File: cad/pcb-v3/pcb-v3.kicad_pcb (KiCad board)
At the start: 4 copper layers, 19.3 x 19.3 mm, 50 parts

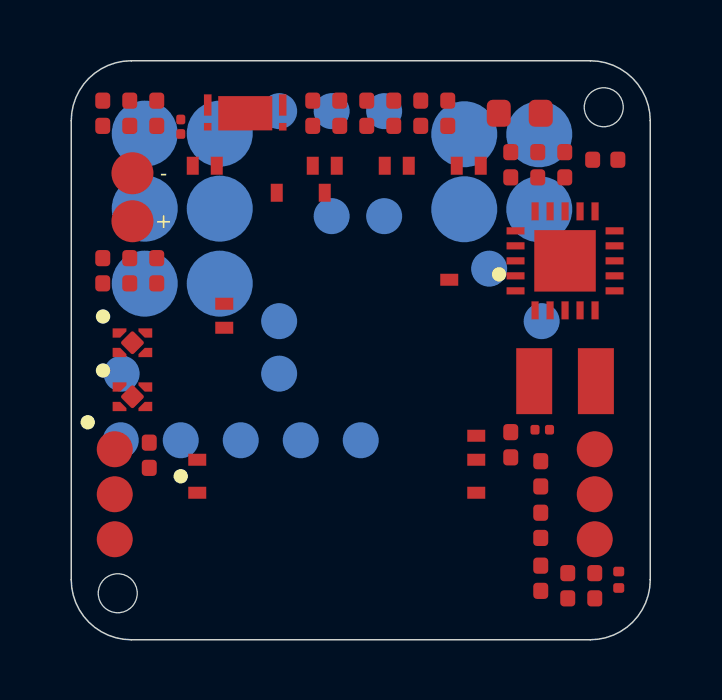
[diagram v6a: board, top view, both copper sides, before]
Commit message: regenerate placement: 20x19 board, caliper pogo datum, press-fit pins
Board is no longer square, so the generator had to learn the difference. Five
SQUARE-BOARD BUGS were hiding behind a single HALF constant, every one of them
silently using an X value where a Y was meant:

  * np.meshgrid(_gx, _gx) built a 20 x 20 grid on a 20 x 19 board
  * the legality mask was np.ones((_NX,_NX)) instead of (_NY,_NX)
  * the index guard tested iy against _NX
  * FIVE sites read _gx[iy] for a Y coordinate -- this is what put a row of
    0402s at y=-9.12, off the board
  * U5's own candidate loop read _gx[_iy], which parked it at y=-8.4 through
    the housing lip wall
  * the Edge.Cuts corner arcs used one  for both axes

None of these could show up while the board was square. BOARD/HALF are now
BOARD_X/BOARD_Y and HALF_X/HALF_Y so the distinction cannot collapse again.

POGO DATUM, from calipers, every measurement closing:
  pad 2.00, pin 1.00, uniform 2.50 pitch (0.50 gap)
  cols x = -6.50, -4.00, +4.00, +6.50   rows y = -8.25, -5.75, -3.25
  board edge -> outer PIN edge 3.00 | between inner PAD edges 6.00
  top PAD edge to -Y edge 0.25 | J4 4.50x7.00 | J11 4.50x4.50
  chain 2.50+4.50+6.00+4.50+2.50 = 20.00 exactly
Pad dia went 2.20 -> 2.00 because the 0.25 edge reading is to the OEM's 2.00
pad; at 2.20 the top row reaches y=-9.35 against a -9.30 limit.

SCREWS -> PRESS-FIT PINS at (-8.75, 0) and (+8.75, 0), i.e. corner-origin
(1.25, 9.50) and (18.75, 9.50) as asked. A pin passes THROUGH the hole, so the
r1.20 plastic boss that used to stand on the board face is gone and the
board-side cost is the hole alone -- which is the only reason these positions
are reachable. BOSS_R is now the hole radius (0.60), not zero: zero would let
the placer park a part on the pin. Hole 1.20 leaves a 0.65 mm web to the edge.

Also fixed a FALSE clearance violation in this file's own checker: it modelled
every pad as an axis-aligned box, which under-reports the gap between two ROUND
pads offset dia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
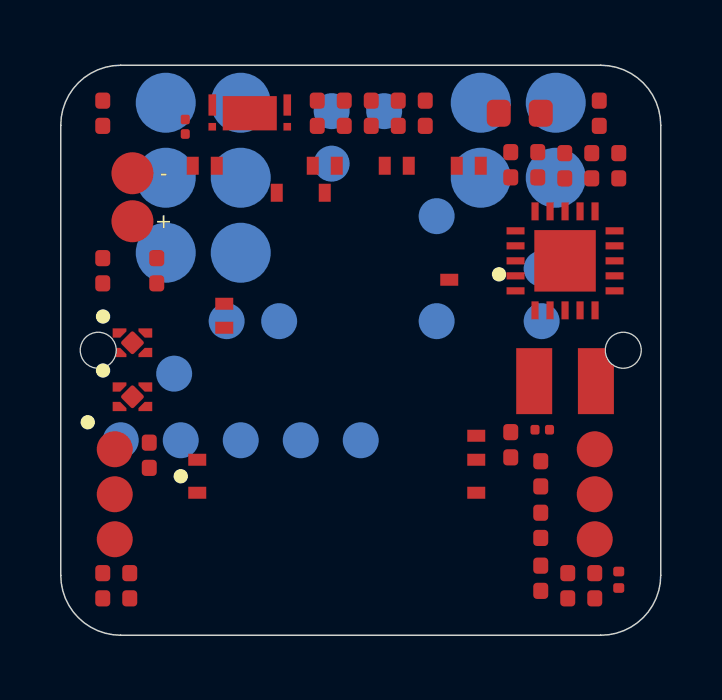
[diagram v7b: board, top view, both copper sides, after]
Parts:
- removed the ? at (8.10, -8.10)
- removed the ? at (-8.10, 8.10)
- added ?: , touchid:MH, F.Cu at (-8.75, 0.00)
- added ?: , touchid:MH, F.Cu at (8.75, 0.00)
- moved R3 18.2 mm to (6.00, 4.12)
- moved R5 17.8 mm to (-8.60, -2.65)
- moved R2 16.5 mm to (7.80, 7.85)
- moved R8 15.7 mm to (6.05, 2.65), turned to 0 degrees
- moved R9 15.6 mm to (-5.85, -7.45), turned to 90 degrees
- moved C3 14.6 mm to (-7.70, 7.85)
- moved ROK1 14.0 mm to (8.60, -6.15)
- moved C5 12.4 mm to (5.00, 3.15)
- moved R1 11.9 mm to (5.00, -6.18)
- moved C12 11.5 mm to (-7.05, 3.50)
- moved R6 9.61 mm to (1.25, -7.90)
- moved R7 8.87 mm to (-0.55, -7.90)
- moved C13 7.00 mm to (-8.60, -7.90)
- moved C10 5.07 mm to (6.90, 7.85)
- moved TP3 4.95 mm to (2.53, -0.97)
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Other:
- board size 19.3 x 19.3 mm -> 20 x 19 mm

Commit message: wire up the PCM cluster constraint that was written but never read
C14 -- the PCM's supply bypass -- was 19.77 mm from U5 on a 20 mm board. Three
things were wrong, all of them latent:

1. SMALL_NEAR = (3.0, 4.5, 6.0, 8.0) existed, and _place_smalls' own comment
   said 'keep them within SMALL_NEAR of U5', but NOTHING EVER READ IT.
   Distance only ever RANKED candidates; it never REJECTED one. With the shelf
   beside U5 full, 'nearest' became the far corner.
2. CLUSTER_OK was 99.0 -- the guard meant to reject a U5 position that
   scatters its cluster was effectively switched off.
3. _place_smalls masked every 0402 SLOT out and hunted leftover space, while
   its own docstring said these parts take slots. There is no leftover space
   next to U5, which is why forcing a radius made every U5 trial fail outright.

Fixed: per-part ladders (C14 tightest, it is the bypass; R8 loosest, its 330
ohm swamps any parasitic), C14 placed FIRST so it takes the best spot rather
than the leftovers, CLUSTER_OK 99 -> 8, and slot centres offered as candidates
with the consumed slot handed back to the packer. Slot candidates are checked
against the real legality mask -- skipping that first put R8 past the 17.94
housing cavity and overlapped C14 with R9.

    C14  19.77 mm -> 3.42     R8  14.31 -> 4.75     R9  2.18 -> 1.95

Routing: PCM_VDD then CELL_NEG then PCM_VM must go BEFORE the rest of stage 1.
With the cluster tight, PCM_VM takes the corridor PCM_VDD needs to reach C14
and PCM_VDD fails. Split into stage 1a (PCM) and 1b (the rest); all route.

New push_off_pads.py: the router lays copper 1-9 microns inside the clearance
rule against ROTATED 0402 pads, on a different net every re-route. Hand-nudging
one segment at a time had been done twice. This finds every grazing track,
computes the shortest perpendicular push, and RE-TESTS the pushed segment
against every foreign pad, track and via before accepting it -- a fix that
trades one violation for another is not a fix. 28 segments p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
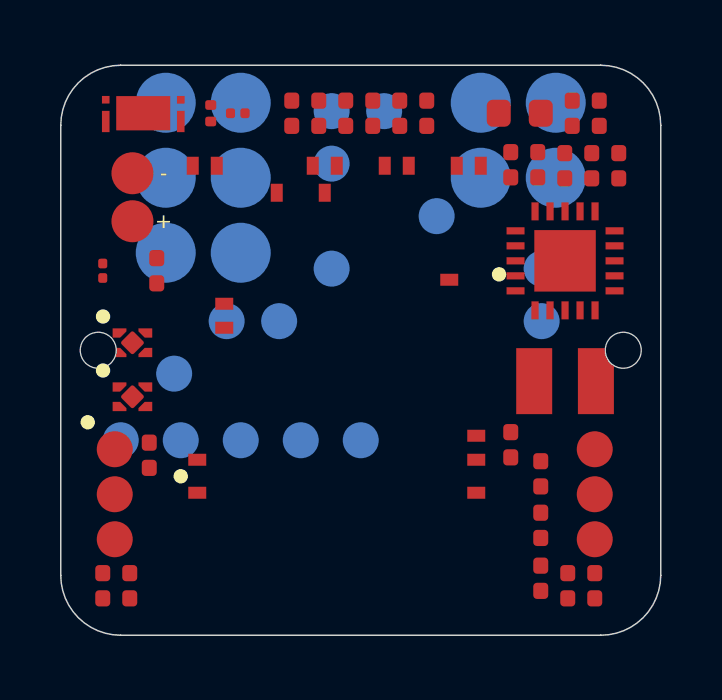
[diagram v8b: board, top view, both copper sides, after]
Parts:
- moved C14 20.7 mm to (-5.00, -7.90)
- moved R8 15.6 mm to (-8.60, -2.65), turned to 90 degrees
- moved R2 14.2 mm to (5.90, -6.18)
- moved C3 13.8 mm to (6.00, 5.84)
- moved R7 12.4 mm to (5.00, 3.15)
- moved C5 12.3 mm to (-0.50, -7.90)
- moved R5 10.5 mm to (-7.70, 7.85)
- moved C13 6.30 mm to (-2.30, -7.90)
- moved TP3 3.91 mm to (-0.97, -2.72)
- moved U5 3.55 mm to (-7.25, -7.90), turned to 180 degrees
- moved C1 2.70 mm to (7.80, 7.85)
- moved R9 1.81 mm to (-4.10, -7.90), turned to 0 degrees
- moved ROK3 1.77 mm to (7.05, -7.90)
- moved C10 0.93 mm to (6.00, 7.60)
- moved C2 0.93 mm to (6.90, 7.85)
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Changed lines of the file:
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@@
 	(footprint "touchid:TP3"
 		(layer "F.Cu")
-		(at 2.53 -0.97)
+		(at -0.97 -2.72)
 		(property "Reference" "TP3"
 			(at 0 0 0)
@@
 	(footprint "touchid:U5"
 		(layer "F.Cu")
-		(at -3.7 -7.9)
+		(at -7.25 -7.9 180)
 		(property "Reference" "U5"
 			(at 0 0 0)
@@
 		)
 	)
+	(footprint "touchid:C14"
+		(layer "F.Cu")
+		(at -5.0 -7.9 90)
+		(property "Reference" "C14"
+			(at 0 0 0)
+			(layer "F.SilkS")
+			(hide yes)
+			(effects (font (size 0.6 0.6) (thickness 0.1)))
+		)
+		(attr smd)
+		(fp_text user "C14"
+			(at 0 0 0)
+			(layer "F.Fab")
+			(effects (font (size 0.4 0.4) (thickness 0.06)))
+		)
+		(pad "1" smd roundrect
+			(at -0.2743 0)
+			(size 0.3684 0.324)
+			(layers "F.Cu" "F.Mask" "F.Paste")
+			(roundrect_rratio 0.25)
+			(net 12 "PCM_VDD")
+		)
+		(pad "2" smd roundrect
+			(at 0.2743 0)
+			(size 0.3684 0.324)
+			(layers "F.Cu" "F.Mask" "F.Paste")
+			(roundrect_rratio 0.25)
+			(net 3 "CELL_NEG")
+		)
+		(model "${KIPRJMOD}/3dmodels/chip_0402.step"
+			(offset (xyz 0 0 0))
+			(scale (xyz 1 1 1))
+			(rotate (xyz 0 0 0))
+		)
+	)
 	(footprint "touchid:R9"
 		(layer "F.Cu")
-		(at -5.85 -7.45 90)
+		(at -4.1 -7.9)
 		(property "Reference" "R9"
 			(at 0 0 0)
@@
 	(footprint "touchid:R8"
 		(layer "F.Cu")
-		(at 6.05 2.65)
+		(at -8.6 -2.65 90)
 		(property "Reference" "R8"
 			(at 0 0 0)
@@
 		)
 	)
-	(footprint "touchid:C14"
-		(layer "F.Cu")
-		(at 8.6 7.65 90)
-		(property "Reference" "C14"
-			(at 0 0 0)
-			(layer "F.SilkS")
-			(hide yes)
-			(effects (font (size 0.6 0.6) (thickness 0.1)))
-		)
-		(attr smd)
-		(fp_text user "C14"
-			(at 0 0 0)
-			(layer "F.Fab")
-			(effects (font (size 0.4 0.4) (thickness 0.06)))
-		)
-		(pad "1" smd roundrect
-			(at -0.2743 0)
-			(size 0.3684 0.324)
-			(layers "F.Cu" "F.Mask" "F.Paste")
-			(roundrect_rratio 0.25)
-			(net 12 "PCM_VDD")
-		)
-		(pad "2" smd roundrect
-			(at 0.2743 0)
-			(size 0.3684 0.324)
-			(layers "F.Cu" "F.Mask" "F.Paste")
-			(roundrect_rratio 0.25)
-			(net 3 "CELL_NEG")
-		)
-		(model "${KIPRJMOD}/3dmodels/chip_0402.step"
-			(offset (xyz 0 0 0))
-			(scale (xyz 1 1 1))
-			(rotate (xyz 0 0 0))
-		)
-	)
 	(footprint "touchid:C1"
 		(layer "F.Cu")
+		(at 7.8 7.85 90)
+		(property "Reference" "C1"
+			(at 0 0 0)
+			(layer "F.SilkS")
+			(hide yes)
+			(effects (font (size 0.6 0.6) (thickness 0.1)))
+		)
+		(attr smd)
+		(fp_text user "C1"
+			(at 0 0 0)
+			(layer "F.Fab")
+			(effects (font (size 0.4 0.4) (thickness 0.06)))
+		)
+		(pad "1" smd roundrect
+			(at -0.42 0)
+			(size 0.5 0.54)
+			(layers "F.Cu" "F.Mask" "F.Paste")
+			(roundrect_rratio 0.25)
+			(net 27 "VIN_DC")
+		)
+		(pad "2" smd roundrect
+			(at 0.42 0)
+			(size 0.5 0.54)
+			(layers "F.Cu" "F.Mask" "F.Paste")
+			(roundrect_rratio 0.25)
+			(net 4 "GND")
+		)
+		(model "${KIPRJMOD}/3dmodels/chip_0402.step"
+			(offset (xyz 0 0 0))
+			(scale (xyz 1 1 1))
+			(rotate (xyz 0 0 0))
+		)
+	)
+	(footprint "touchid:C2"
+		(layer "F.Cu")
+		(at 6.9 7.85 90)
+		(property "Reference" "C2"
+			(at 0 0 0)
+			(layer "F.SilkS")
+			(hide yes)
+			(effects (font (size 0.6 0.6) (thickness 0.1)))
+		)
+		(attr smd)
+		(fp_text user "C2"
+			(at 0 0 0)
+			(layer "F.Fab")
+			(effects (font (size 0.4 0.4) (thickness 0.06)))
+		)
+		(pad "1" smd roundrect
+			(at -0.42 0)
+			(size 0.5 0.54)
+			(layers "F.Cu" "F.Mask" "F.Paste")
+			(roundrect_rratio 0.25)
+			(net 30 "VSTOR")
+		)
+		(pad "2" smd roundrect
+			(at 0.42 0)
+			(size 0.5 0.54)
+			(layers "F.Cu" "F.Mask" "F.Paste")
+			(roundrect_rratio 0.25)
+			(net 4 "GND")
+		)
+		(model "${KIPRJMOD}/3dmodels/chip_0402.step"
+			(offset (xyz 0 0 0))
+			(scale (xyz 1 1 1))
+			(rotate (xyz 0 0 0))
+		)
+	)
+	(footprint "touchid:C3"
+		(layer "F.Cu")
 		(at 6.0 5.836 90)
-		(property "Reference" "C1"
-			(at 0 0 0)
-			(layer "F.SilkS")
-			(hide yes)
-			(effects (font (size 0.6 0.6) (thickness 0.1)))
-		)
-		(attr smd)
-		(fp_text user "C1"
-			(at 0 0 0)
-			(layer "F.Fab")
-			(effects (font (size 0.4 0.4) (thickness 0.06)))
-		)
-		(pad "1" smd roundrect
-			(at -0.42 0)
-			(size 0.5 0.54)
-			(layers "F.Cu" "F.Mask" "F.Paste")
-			(roundrect_rratio 0.25)
-			(net 27 "VIN_DC")
-		)
-		(pad "2" smd roundrect
-			(at 0.42 0)
-			(size 0.5 0.54)
-			(layers "F.Cu" "F.Mask" "F.Paste")
-			(roundrect_rratio 0.25)
-			(net 4 "GND")
-		)
-		(model "${KIPRJMOD}/3dmodels/chip_0402.step"
-			(offset (xyz 0 0 0))
-			(scale (xyz 1 1 1))
-			(rotate (xyz 0 0 0))
-		)
-	)
-	(footprint "touchid:C2"
-		(layer "F.Cu")
-		(at 6.0 7.6 90)
-		(property "Reference" "C2"
-			(at 0 0 0)
-			(layer "F.SilkS")
-			(hide yes)
-			(effects (font (size 0.6 0.6) (thickness 0.1)))
-		)
-		(attr smd)
-		(fp_text user "C2"
+		(property "Reference" "C3"
+			(at 0 0 0)
+			(layer "F.SilkS")
+			(hide yes)
+			(effects (font (size 0.6 0.6) (thickness 0.1)))
+		)
+		(attr smd)
+		(fp_text user "C3"
 			(at 0 0 0)
 			(layer "F.Fab")
@@
 		)
 	)
-	(footprint "touchid:C3"
-		(layer "F.Cu")
-		(at -7.7 7.85 90)
-		(property "Reference" "C3"
-			(at 0 0 0)
-			(layer "F.SilkS")
-			(hide yes)
-			(effects (font (size 0.6 0.6) (thickness 0.1)))
-		)
-		(attr smd)
-		(fp_text user "C3"
-			(at 0 0 0)
-			(layer "F.Fab")
-			(effects (font (size 0.4 0.4) (thickness 0.06)))
-		)
-		(pad "1" smd roundrect
-			(at -0.42 0)
-			(size 0.5 0.54)
-			(layers "F.Cu" "F.Mask" "F.Paste")
-			(roundrect_rratio 0.25)
-			(net 30 "VSTOR")
-		)
-		(pad "2" smd roundrect
-			(at 0.42 0)
-			(size 0.5 0.54)
-			(layers "F.Cu" "F.Mask" "F.Paste")
-			(roundrect_rratio 0.25)
-			(net 4 "GND")
-		)
-		(model "${KIPRJMOD}/3dmodels/chip_0402.step"
-			(offset (xyz 0 0 0))
-			(scale (xyz 1 1 1))
-			(rotate (xyz 0 0 0))
-		)
-	)
 	(footprint "touchid:C4"
 		(layer "F.Cu")
-		(at 2.15 -7.9 90)
+		(at 2.2 -7.9 90)
 		(property "Reference" "C4"
 			(at 0 0 0)
@@
 	(footprint "touchid:C5"
 		(layer "F.Cu")
-		(at 5.0 3.15 90)
+		(at -0.5 -7.9 90)
 		(property "Reference" "C5"
 			(at 0 0 0)
@@
 	(footprint "touchid:C6"
 		(layer "F.Cu")
-		(at -1.45 -7.9 90)
+		(at -1.4 -7.9 90)
 		(property "Reference" "C6"
 			(at 0 0 0)
@@
 	(footprint "touchid:C9"
 		(layer "F.Cu")
-		(at 0.35 -7.9 90)
+		(at 0.4 -7.9 90)
 		(property "Reference" "C9"
 			(at 0 0 0)
@@
 	(footprint "touchid:C10"
 		(layer "F.Cu")
-		(at 6.9 7.85 90)
+		(at 6.0 7.6 90)
 		(property "Reference" "C10"
 			(at 0 0 0)
@@
 	(footprint "touchid:C13"
 		(layer "F.Cu")
-		(at -8.6 -7.9 90)
+		(at -2.3 -7.9 90)
 		(property "Reference" "C13"
 			(at 0 0 0)
@@
 	(footprint "touchid:R2"
 		(layer "F.Cu")
-		(at 7.8 7.85 90)
+		(at 5.9 -6.183 90)
 		(property "Reference" "R2"
 			(at 0 0 0)
@@
 	(footprint "touchid:R5"
 		(layer "F.Cu")
-		(at -8.6 -2.65 90)
+		(at -7.7 7.85 90)
 		(property "Reference" "R5"
 			(at 0 0 0)
@@
 	(footprint "touchid:R6"
 		(layer "F.Cu")
-		(at 1.25 -7.9 90)
+		(at 1.3 -7.9 90)
 		(property "Reference" "R6"
 			(at 0 0 0)
@@
 	(footprint "touchid:R7"
 		(layer "F.Cu")
-		(at -0.55 -7.9 90)
+		(at 5.0 3.15 90)
 		(property "Reference" "R7"
 			(at 0 0 0)
@@
 	(footprint "touchid:ROV2"
 		(layer "F.Cu")
-		(at 5.9 -6.183 90)
+		(at 6.8 -6.15 90)
 		(property "Reference" "ROV2"
 			(at 0 0 0)
@@
 	(footprint "touchid:ROK3"
 		(layer "F.Cu")
-		(at 6.8 -6.15 90)
+		(at 7.05 -7.9 90)
 		(property "Reference" "ROK3"
 			(at 0 0 0)
